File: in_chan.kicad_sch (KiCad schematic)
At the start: 8 parts, among them U8 MAX31910AUI+

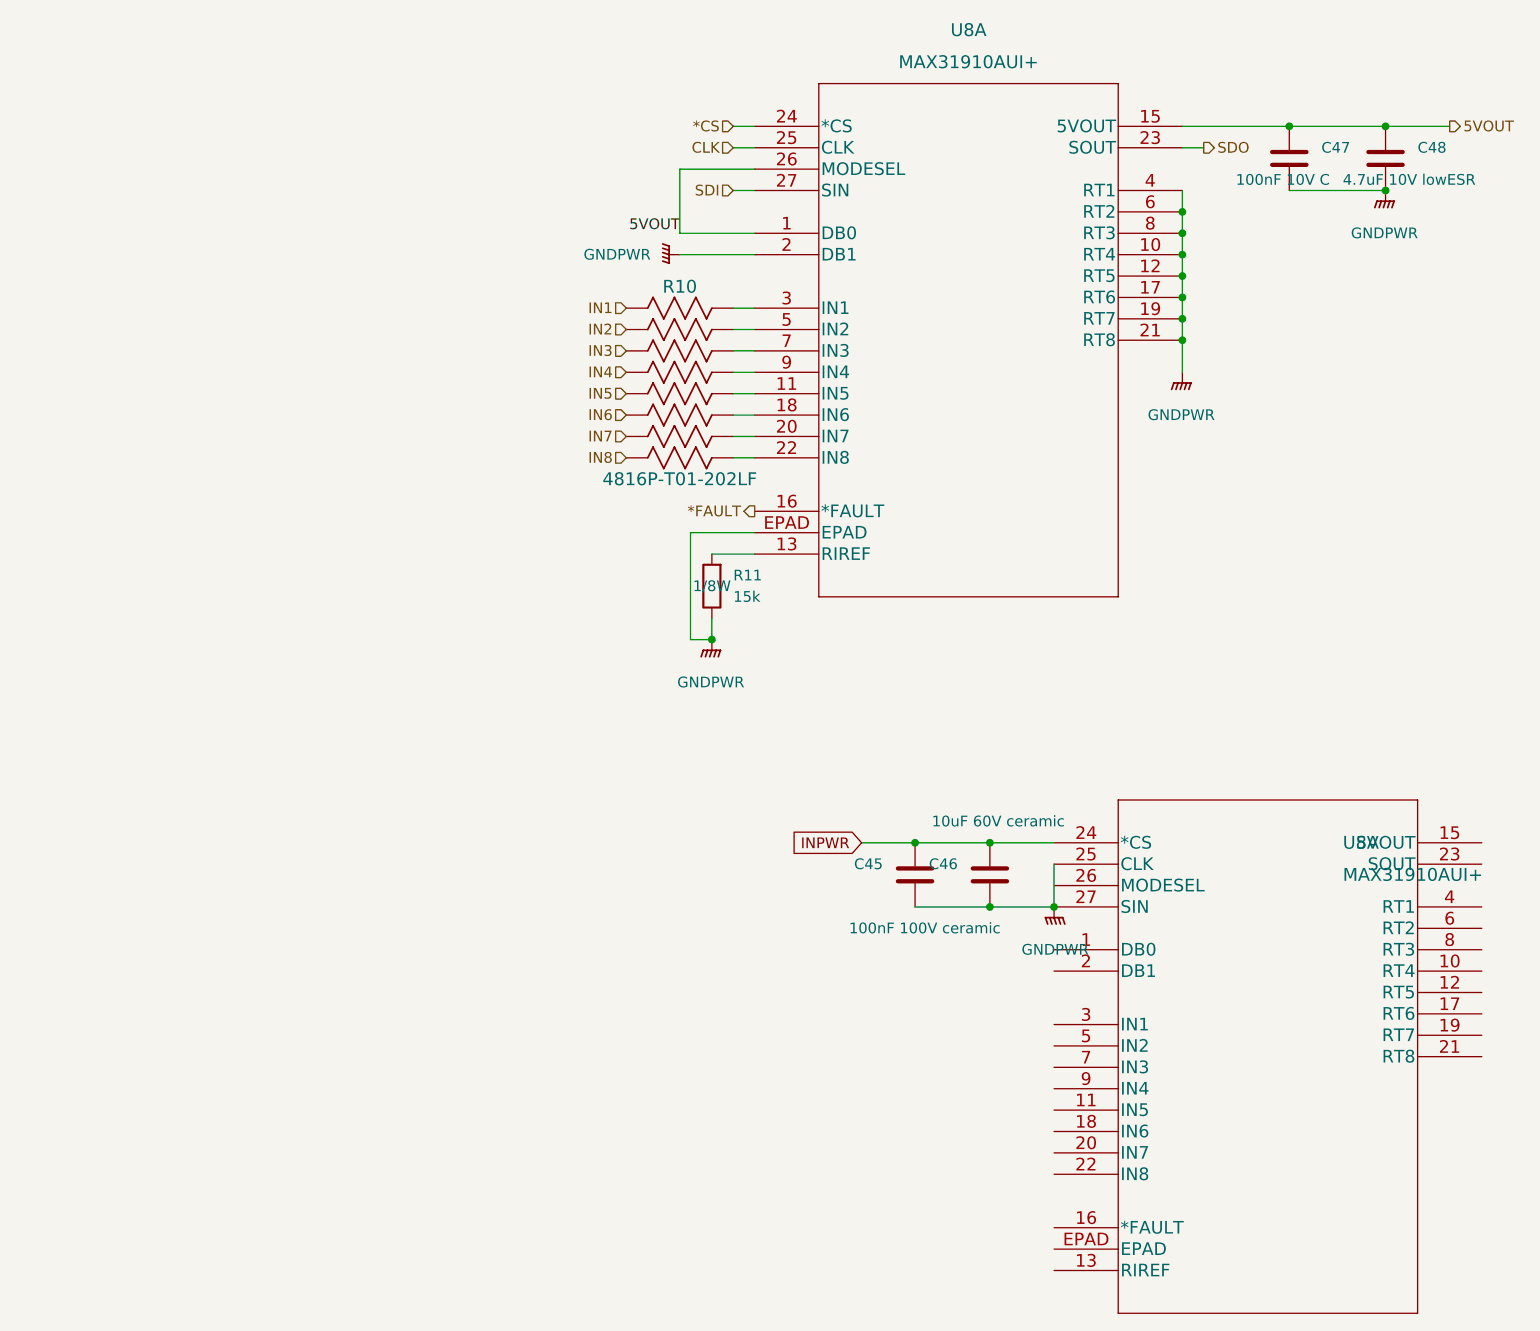
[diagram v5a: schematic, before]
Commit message: change package QFN => MSOP
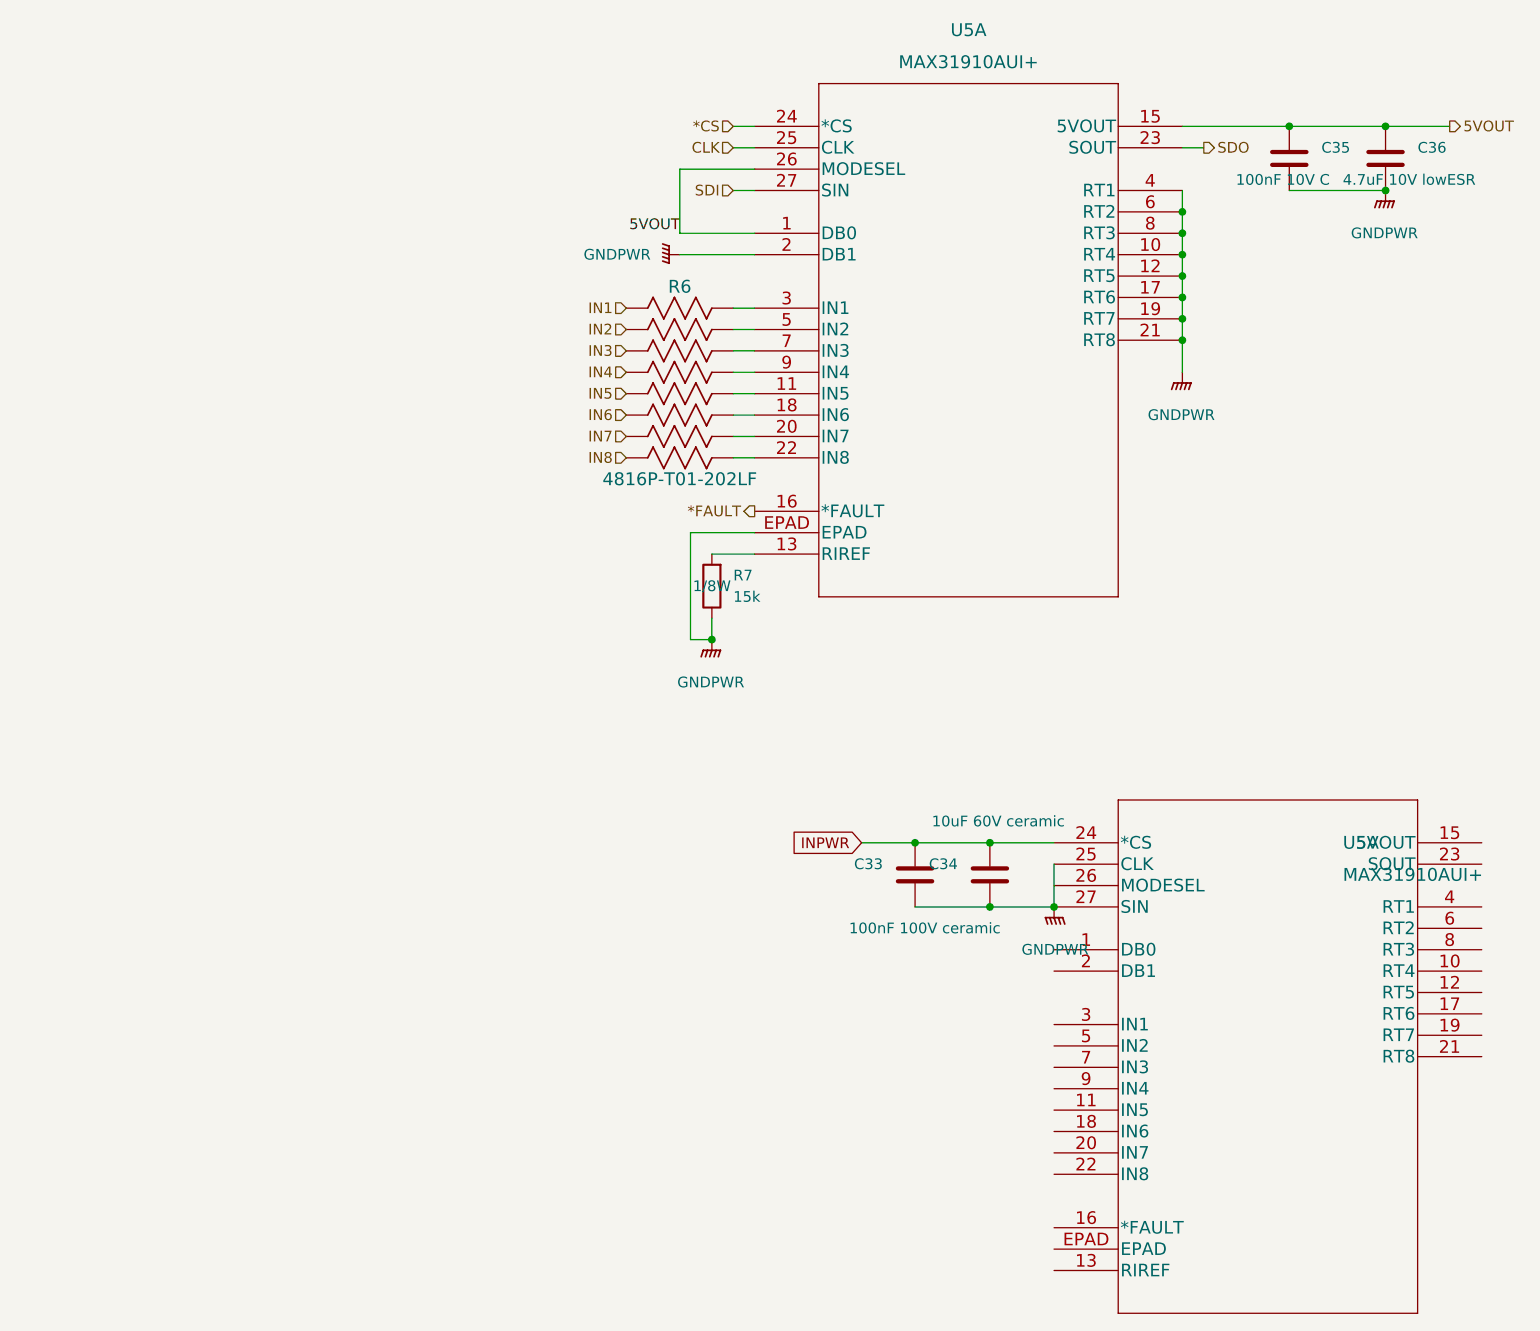
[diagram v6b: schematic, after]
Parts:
- renumbered C45 to C33, C46 to C34, C47 to C35, C48 to C36, R10 to R6, R11 to R7, U8 to U5
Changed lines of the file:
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@@
   (symbol (lib_id "power:GNDPWR") (at 163.83 119.38 0)
     (in_bom yes) (on_board yes) (fields_autoplaced)
-    (property "Reference" "#PWR051" (id 0) (at 163.83 124.46 0)
+    (property "Reference" "#PWR031" (id 0) (at 163.83 124.46 0)
       (effects (font (size 1.27 1.27)) hide)
     )
@@
   (symbol (lib_id "Device:R") (at 163.83 113.03 180)
     (in_bom yes) (on_board yes)
-    (property "Reference" "R11" (id 0) (at 166.37 111.76 0)
+    (property "Reference" "R7" (id 0) (at 166.37 111.76 0)
       (effects (font (size 1.27 1.27)) (justify right))
     )
@@
   (symbol (lib_id "power:GNDPWR") (at 204.47 151.13 0) (mirror y)
     (in_bom yes) (on_board yes) (fields_autoplaced)
-    (property "Reference" "#PWR052" (id 0) (at 204.47 156.21 0)
+    (property "Reference" "#PWR032" (id 0) (at 204.47 156.21 0)
       (effects (font (size 1.27 1.27)) hide)
     )
@@
   (symbol (lib_id "power:GNDPWR") (at 243.84 66.04 0)
     (in_bom yes) (on_board yes) (fields_autoplaced)
-    (property "Reference" "#PWR054" (id 0) (at 243.84 71.12 0)
+    (property "Reference" "#PWR034" (id 0) (at 243.84 71.12 0)
       (effects (font (size 1.27 1.27)) hide)
     )
@@
   (symbol (lib_id "Device:C") (at 243.84 62.23 0)
     (in_bom yes) (on_board yes)
-    (property "Reference" "C48" (id 0) (at 247.65 60.9599 0)
+    (property "Reference" "C36" (id 0) (at 247.65 60.9599 0)
       (effects (font (size 1.27 1.27)) (justify left))
     )
@@
   (symbol (lib_id "Maxim industrial IO:MAX31910AUI+") (at 204.47 143.51 0)
     (in_bom yes) (on_board yes) (fields_autoplaced)
-    (property "Reference" "U8" (id 0) (at 238.76 143.51 0)
+    (property "Reference" "U5" (id 0) (at 238.76 143.51 0)
       (effects (font (size 1.524 1.524)) (justify left))
     )
@@
   (symbol (lib_id "Device:C") (at 187.96 147.32 0) (mirror y)
     (in_bom yes) (on_board yes)
-    (property "Reference" "C45" (id 0) (at 184.15 146.0499 0)
+    (property "Reference" "C33" (id 0) (at 184.15 146.0499 0)
       (effects (font (size 1.27 1.27)) (justify left))
     )
@@
   (symbol (lib_id "power:GNDPWR") (at 219.71 87.63 0)
     (in_bom yes) (on_board yes) (fields_autoplaced)
-    (property "Reference" "#PWR053" (id 0) (at 219.71 92.71 0)
+    (property "Reference" "#PWR033" (id 0) (at 219.71 92.71 0)
       (effects (font (size 1.27 1.27)) hide)
     )
@@
   (symbol (lib_id "Device:C") (at 232.41 62.23 0)
     (in_bom yes) (on_board yes)
-    (property "Reference" "C47" (id 0) (at 236.22 60.9599 0)
+    (property "Reference" "C35" (id 0) (at 236.22 60.9599 0)
       (effects (font (size 1.27 1.27)) (justify left))
     )
@@
   (symbol (lib_id "power:GNDPWR") (at 160.02 73.66 270)
     (in_bom yes) (on_board yes)
-    (property "Reference" "#PWR050" (id 0) (at 154.94 73.66 0)
+    (property "Reference" "#PWR030" (id 0) (at 154.94 73.66 0)
       (effects (font (size 1.27 1.27)) hide)
     )
@@
   (symbol (lib_id "Device:C") (at 196.85 147.32 0) (mirror y)
     (in_bom yes) (on_board yes)
-    (property "Reference" "C46" (id 0) (at 193.04 146.0499 0)
+    (property "Reference" "C34" (id 0) (at 193.04 146.0499 0)
       (effects (font (size 1.27 1.27)) (justify left))
     )
@@
   (symbol (lib_id "Num-IO:4816P-T01-103LF") (at 153.67 80.01 0)
     (in_bom yes) (on_board yes)
-    (property "Reference" "R10" (id 0) (at 160.02 77.47 0)
+    (property "Reference" "R6" (id 0) (at 160.02 77.47 0)
       (effects (font (size 1.524 1.524)))
     )
@@
   (symbol (lib_id "Maxim industrial IO:MAX31910AUI+") (at 168.91 58.42 0)
     (in_bom yes) (on_board yes) (fields_autoplaced)
-    (property "Reference" "U8" (id 0) (at 194.31 46.99 0)
-      (effects (font (size 1.524 1.524)))
-    )
+    (property "Reference" "U5" (id 0) (at 194.31 46.99 0)
+      (effects (font (size 1.524 1.524)))
+    )

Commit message: add missing LDO for 3.3V
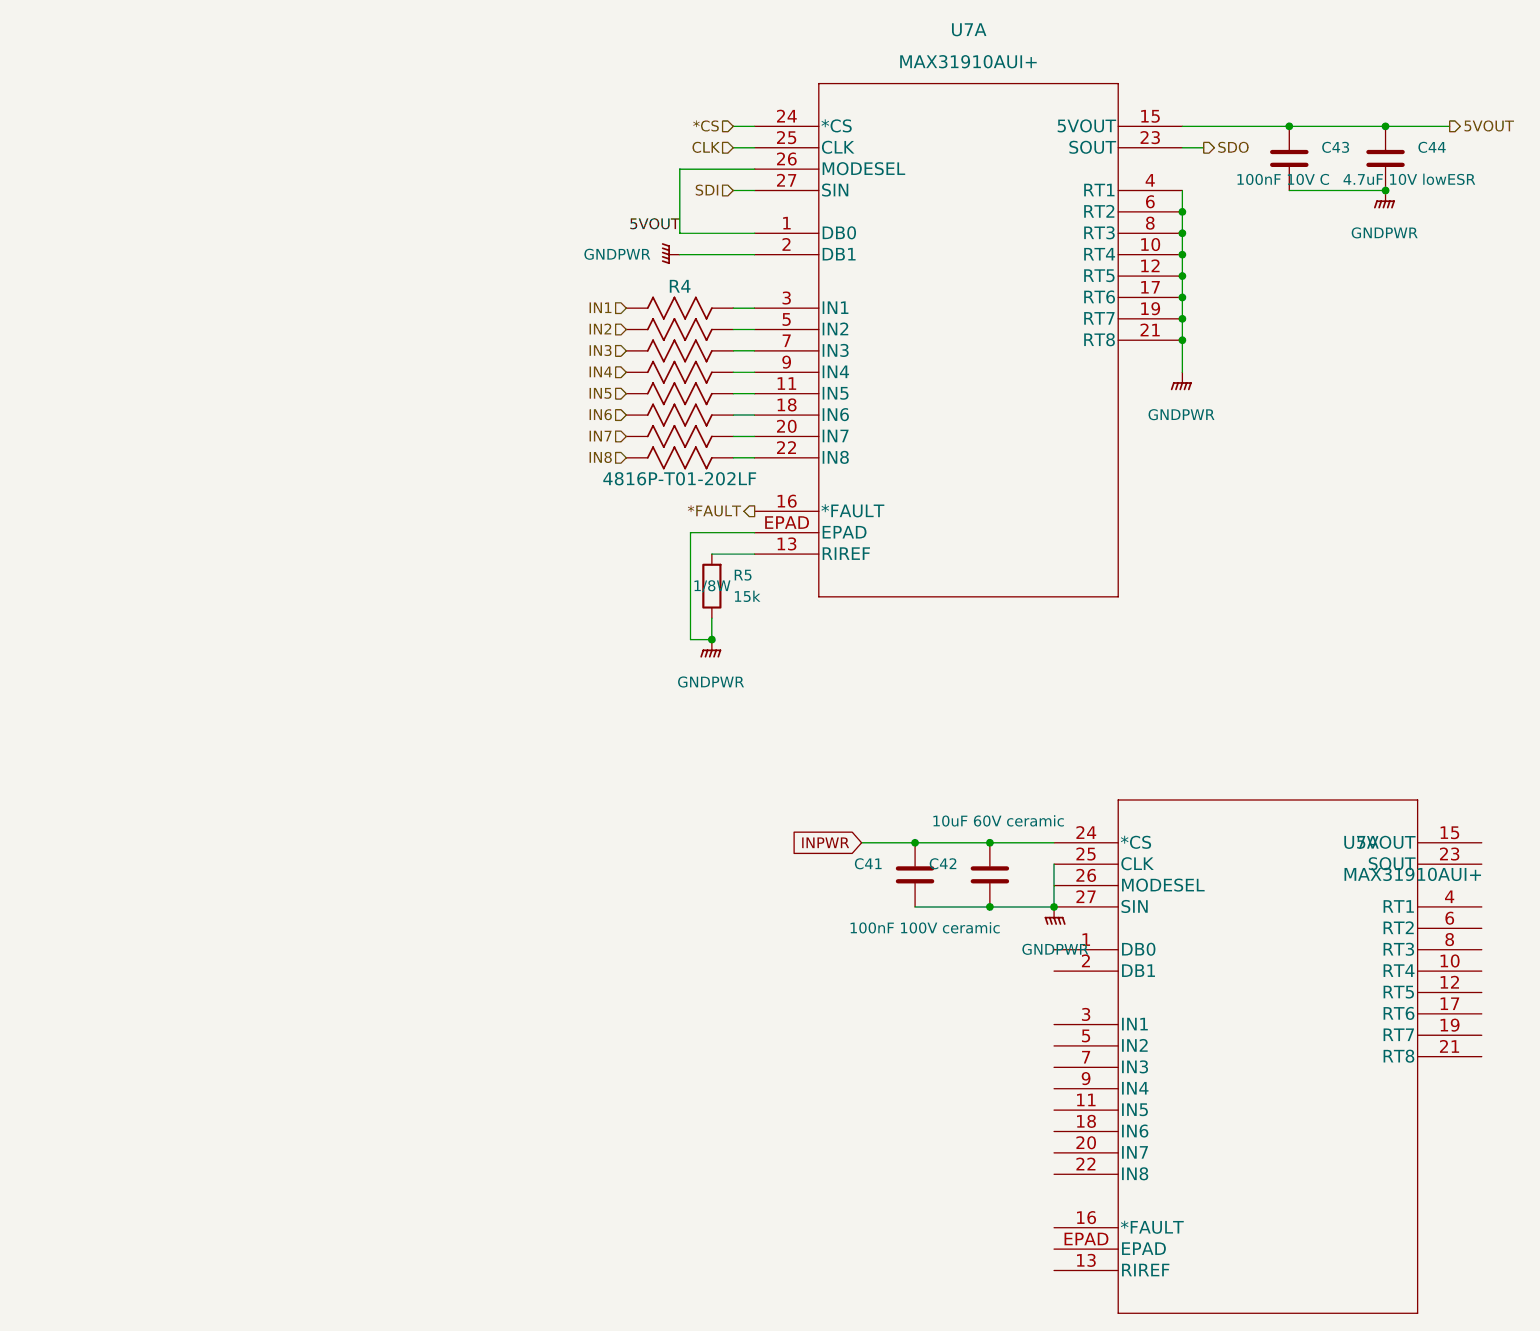
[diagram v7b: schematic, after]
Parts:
- renumbered C33 to C41, C34 to C42, C35 to C43, C36 to C44, R6 to R4, R7 to R5, U5 to U7
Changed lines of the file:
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@@
   (symbol (lib_id "power:GNDPWR") (at 163.83 119.38 0)
     (in_bom yes) (on_board yes) (fields_autoplaced)
-    (property "Reference" "#PWR031" (id 0) (at 163.83 124.46 0)
+    (property "Reference" "#PWR051" (id 0) (at 163.83 124.46 0)
       (effects (font (size 1.27 1.27)) hide)
     )
@@
   (symbol (lib_id "Device:R") (at 163.83 113.03 180)
     (in_bom yes) (on_board yes)
-    (property "Reference" "R7" (id 0) (at 166.37 111.76 0)
+    (property "Reference" "R5" (id 0) (at 166.37 111.76 0)
       (effects (font (size 1.27 1.27)) (justify right))
     )
@@
   (symbol (lib_id "power:GNDPWR") (at 204.47 151.13 0) (mirror y)
     (in_bom yes) (on_board yes) (fields_autoplaced)
-    (property "Reference" "#PWR032" (id 0) (at 204.47 156.21 0)
+    (property "Reference" "#PWR052" (id 0) (at 204.47 156.21 0)
       (effects (font (size 1.27 1.27)) hide)
     )
@@
   (symbol (lib_id "power:GNDPWR") (at 243.84 66.04 0)
     (in_bom yes) (on_board yes) (fields_autoplaced)
-    (property "Reference" "#PWR034" (id 0) (at 243.84 71.12 0)
+    (property "Reference" "#PWR054" (id 0) (at 243.84 71.12 0)
       (effects (font (size 1.27 1.27)) hide)
     )
@@
   (symbol (lib_id "Device:C") (at 243.84 62.23 0)
     (in_bom yes) (on_board yes)
-    (property "Reference" "C36" (id 0) (at 247.65 60.9599 0)
+    (property "Reference" "C44" (id 0) (at 247.65 60.9599 0)
       (effects (font (size 1.27 1.27)) (justify left))
     )
@@
   (symbol (lib_id "Maxim industrial IO:MAX31910AUI+") (at 204.47 143.51 0)
     (in_bom yes) (on_board yes) (fields_autoplaced)
-    (property "Reference" "U5" (id 0) (at 238.76 143.51 0)
+    (property "Reference" "U7" (id 0) (at 238.76 143.51 0)
       (effects (font (size 1.524 1.524)) (justify left))
     )
@@
   (symbol (lib_id "Device:C") (at 187.96 147.32 0) (mirror y)
     (in_bom yes) (on_board yes)
-    (property "Reference" "C33" (id 0) (at 184.15 146.0499 0)
+    (property "Reference" "C41" (id 0) (at 184.15 146.0499 0)
       (effects (font (size 1.27 1.27)) (justify left))
     )
@@
   (symbol (lib_id "power:GNDPWR") (at 219.71 87.63 0)
     (in_bom yes) (on_board yes) (fields_autoplaced)
-    (property "Reference" "#PWR033" (id 0) (at 219.71 92.71 0)
+    (property "Reference" "#PWR053" (id 0) (at 219.71 92.71 0)
       (effects (font (size 1.27 1.27)) hide)
     )
@@
   (symbol (lib_id "Device:C") (at 232.41 62.23 0)
     (in_bom yes) (on_board yes)
-    (property "Reference" "C35" (id 0) (at 236.22 60.9599 0)
+    (property "Reference" "C43" (id 0) (at 236.22 60.9599 0)
       (effects (font (size 1.27 1.27)) (justify left))
     )
@@
   (symbol (lib_id "power:GNDPWR") (at 160.02 73.66 270)
     (in_bom yes) (on_board yes)
-    (property "Reference" "#PWR030" (id 0) (at 154.94 73.66 0)
+    (property "Reference" "#PWR050" (id 0) (at 154.94 73.66 0)
       (effects (font (size 1.27 1.27)) hide)
     )
@@
   (symbol (lib_id "Device:C") (at 196.85 147.32 0) (mirror y)
     (in_bom yes) (on_board yes)
-    (property "Reference" "C34" (id 0) (at 193.04 146.0499 0)
+    (property "Reference" "C42" (id 0) (at 193.04 146.0499 0)
       (effects (font (size 1.27 1.27)) (justify left))
     )
@@
   (symbol (lib_id "Num-IO:4816P-T01-103LF") (at 153.67 80.01 0)
     (in_bom yes) (on_board yes)
-    (property "Reference" "R6" (id 0) (at 160.02 77.47 0)
+    (property "Reference" "R4" (id 0) (at 160.02 77.47 0)
       (effects (font (size 1.524 1.524)))
     )
@@
   (symbol (lib_id "Maxim industrial IO:MAX31910AUI+") (at 168.91 58.42 0)
     (in_bom yes) (on_board yes) (fields_autoplaced)
-    (property "Reference" "U5" (id 0) (at 194.31 46.99 0)
-      (effects (font (size 1.524 1.524)))
-    )
+    (property "Reference" "U7" (id 0) (at 194.31 46.99 0)
+      (effects (font (size 1.524 1.524)))
+    )
